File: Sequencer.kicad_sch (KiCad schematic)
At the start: 53 parts, among them J1 Screw_Terminal_01x12, J2 Serial_Mode, J3 USB_C_Receptacle_USB2.0_16P, J4 Extra, U1 ATtiny1616-S, U2 TLP3123, U3 TLP3123, U4 TLP3123, U5 TLP3123, U6 MC78L05_SOT89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

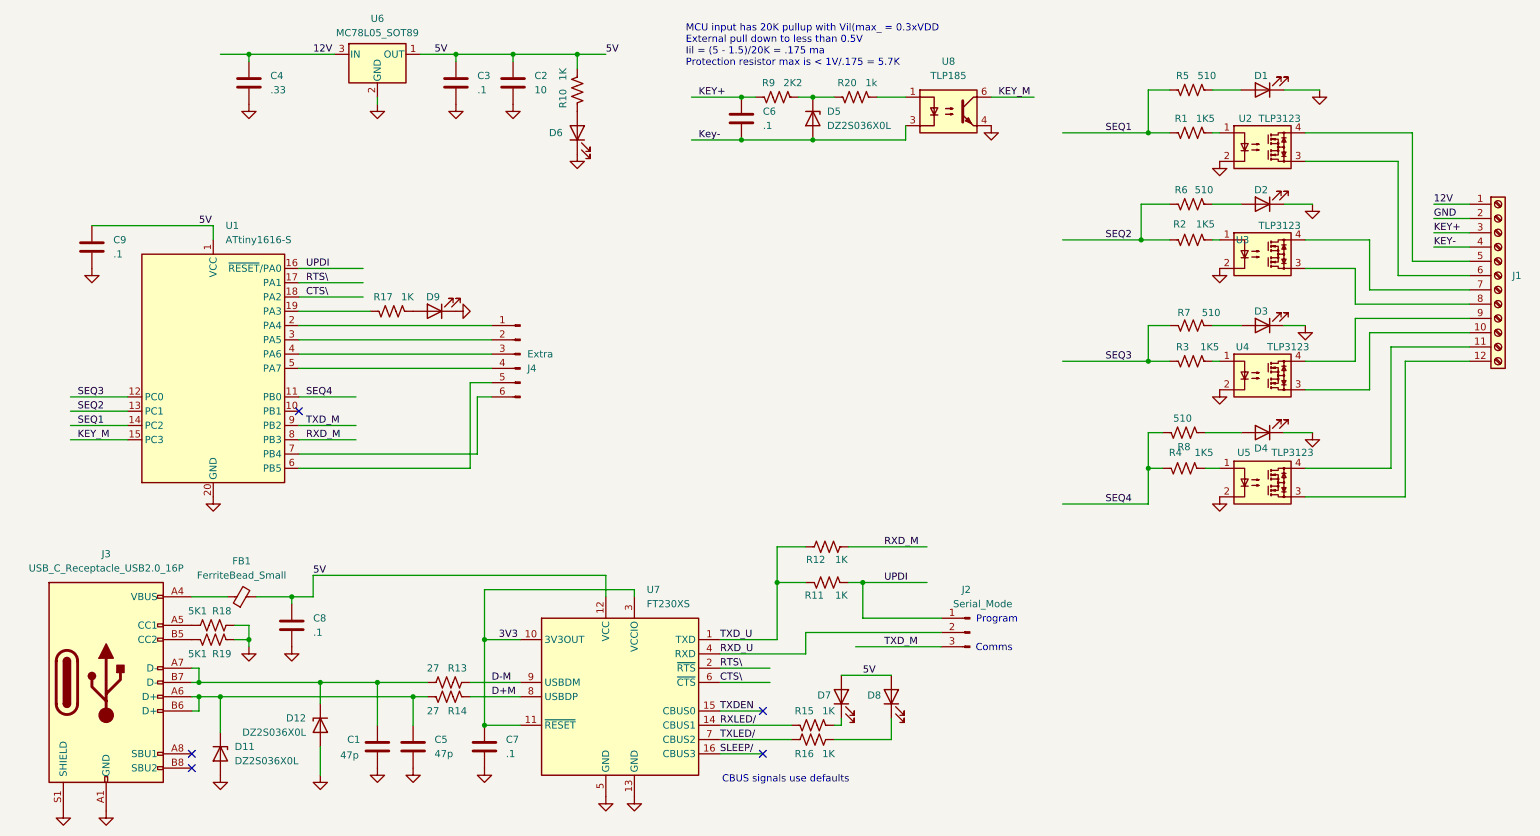
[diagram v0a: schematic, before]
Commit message: Finalized design for release to JCLPCB Add terminal block library Added some data sheets for terminal block, USB-C connector, etc
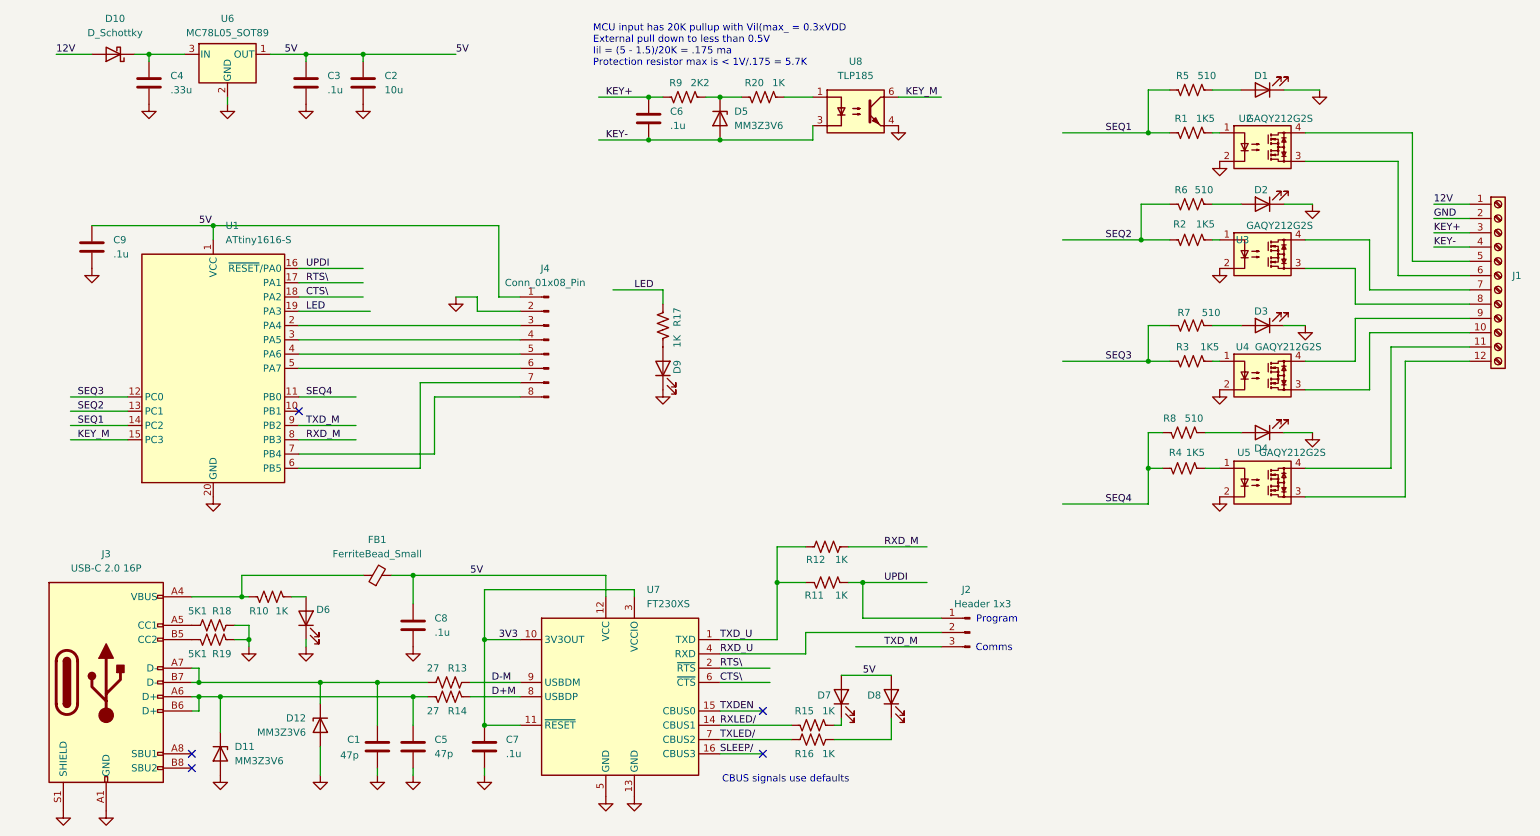
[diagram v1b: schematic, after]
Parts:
- removed J4: Extra, Connector_PinHeader_2.54mm:PinHeader_1x06_P2.54mm_Vertical, symbol Connector:Conn_01x06_Pin
- added D10: D_Schottky, Diode_SMD:D_0603_1608Metric, symbol Device:D_Schottky
- added J4: Conn_01x08_Pin, Connector_PinHeader_2.54mm:PinHeader_1x08_P2.54mm_Vertical, symbol Connector:Conn_01x08_Pin
- C1, C5: LCSC PN (none) -> C1671
- C2: value 10 -> 10u; LCSC PN (none) -> C19702
- C3, C6, C7, C8, C9: value .1 -> .1u; LCSC PN (none) -> C15849
- C4: value .33 -> .33u; LCSC PN (none) -> C2918485
- D1, D2, D3, D4: LCSC PN (none) -> C2286
- D11, D12, D5: value DZ2S036X0L -> MM3Z3V6; footprint Diode_SMD:D_SOD-523 -> Diode_SMD:D_SOD-323; LCSC PN (none) -> C19077454
- D6, D9: LCSC PN (none) -> C22371299
- D7, D8: LCSC PN (none) -> C72038
- FB1: LCSC PN (none) -> C1017
- J1: LCSC PN (none) -> C474929
- J2: value Serial_Mode -> Header 1x3; LCSC PN (none) -> C6332196
- J3: value USB_C_Receptacle_USB2.0_16P -> USB-C 2.0 16P; LCSC PN (none) -> C2835315
- R1, R2, R3, R4: LCSC PN (none) -> C22843
- R10, R11, R12, R15, R16, R17: LCSC PN (none) -> C21190
- R13, R14: LCSC PN (none) -> C25190
- R18, R19: LCSC PN (none) -> C23186
- R20: value 1k -> 1K; LCSC PN (none) -> C21190
- R5, R6, R7, R8: LCSC PN (none) -> C23193
- R9: LCSC PN (none) -> C4190
- U1: LCSC PN (none) -> C614136
- U2, U3, U4, U5: value TLP3123 -> GAQY212G2S; LCSC PN (none) -> C7435109
- U6: LCSC PN (none) -> C5346137
- U7: LCSC PN (none) -> C69082
- U8: LCSC PN (none) -> C17695768
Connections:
- net Key- is gone; now on net KEY-: C6.2, D5.2 (A), U8.3
- net 12V: now also D10.2 (A); no longer C4.1, U6.3 (IN)
- net 5V: now also J4.1 (Pin_1); no longer R10.2
- net GND: now also J4.2 (Pin_2)
- net LED: now reaches R17.1, U1.19 (PA3)
- net at U1.2 (PA4): now also J4.3 (Pin_3)
- net at U1.3 (PA5): now also J4.4 (Pin_4)
- net at U1.4 (PA6): now also J4.5 (Pin_5)
- net at U1.5 (PA7): now also J4.6 (Pin_6)
- net at U1.6 (PB5): now also J4.7 (Pin_7)
- net at U1.7 (PB4): now also J4.8 (Pin_8)
- net at FB1.1, J3.A4 (VBUS), J3.A9 (VBUS)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: now also R10.2
- new net: C4.1, D10.1 (K), U6.3 (IN)
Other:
- moved on the sheet: C2, C3, C4, C6, C8, D5, D6, FB1, R10, R20, R9, U6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

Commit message: Added USB-C connector footprints Changed ATTiny from SOIC-20 to 3x3 mm QFP
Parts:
- removed U1: ATtiny1616-S, Package_SO:SOIC-20W_7.5x12.8mm_P1.27mm, symbol MCU_Microchip_ATtiny:ATtiny1616-S
- added U9: ATtiny1616-M, Package_DFN_QFN:VQFN-20-1EP_3x3mm_P0.4mm_EP1.7x1.7mm, symbol MCU_Microchip_ATtiny:ATtiny1616-M
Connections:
- net 5V: now also U9.4 (VCC)
- net CTS\: now also U9.1 (PA2)
- net GND: now also R17.2, U9.21 (GND), U9.3 (GND); no longer D9.1 (K)
- net KEY_M: now also U9.18 (PC3)
- net LED: now also D9.2 (A), U9.2 (PA3); no longer R17.1
- net RTS\: now also U9.20 (PA1)
- net RXD_M: now also U9.11 (PB3)
- net SEQ1: now also U9.17 (PC2)
- net SEQ2: now also U9.16 (PC1)
- net SEQ3: now also U9.15 (PC0)
- net SEQ4: now also U9.14 (PB0)
- net TXD_M: now also U9.12 (PB2)
- net UPDI: now also U9.19 (~{RESET}/PA0)
- net X1: now reaches J4.3 (Pin_3)
- net X1: now also U9.5 (PA4)
- net X2: now reaches J4.4 (Pin_4)
- net X2: now also U9.6 (PA5)
- net X3: now reaches J4.5 (Pin_5)
- net X3: now also U9.7 (PA6)
- net X4: now reaches J4.6 (Pin_6)
- net X4: now also U9.8 (PA7)
- net X5: now reaches J4.7 (Pin_7)
- net X5: now also U9.9 (PB5)
- net X6: now reaches J4.8 (Pin_8)
- net X6: now also U9.10 (PB4)
- new net: D9.1 (K), R17.1
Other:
- moved on the sheet: D9, R17
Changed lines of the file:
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@@
 	(wire
 		(pts
-			(xy 129.54 66.04) (xy 129.54 68.58)
-		)
-		(stroke
-			(width 0)
-			(type default)
-		)
-	)
-	(wire
-		(pts
 			(xy 64.77 92.71) (xy 74.93 92.71)
 		)
@@
 	(wire
 		(pts
-			(xy 49.53 54.61) (xy 100.33 54.61)
+			(xy 49.53 54.61) (xy 99.06 54.61)
 		)
 		(stroke
@@
 	(wire
 		(pts
+			(xy 129.54 73.66) (xy 129.54 76.2)
+		)
+		(stroke
+			(width 0)
+			(type default)
+		)
+	)
+	(wire
+		(pts
 			(xy 151.13 31.75) (xy 156.21 31.75)
 		)
@@
 	(wire
 		(pts
-			(xy 100.33 67.31) (xy 104.14 67.31)
+			(xy 99.06 67.31) (xy 104.14 67.31)
 		)
 		(stroke
@@
 	(wire
 		(pts
-			(xy 100.33 54.61) (xy 100.33 67.31)
+			(xy 99.06 54.61) (xy 99.06 67.31)
 		)
 		(stroke
@@
 		)
 	)
+	(label "X5"
+		(at 100.33 82.55 0)
+		(fields_autoplaced yes)
+		(effects
+			(font
+				(size 1.27 1.27)
+			)
+			(justify left bottom)
+		)
+	)
 	(label "3V3"
 		(at 100.33 128.27 0)
@@
 		)
 	)
+	(label "X1"
+		(at 100.33 72.39 0)
+		(fields_autoplaced yes)
+		(effects
+			(font
+				(size 1.27 1.27)
+			)
+			(justify left bottom)
+		)
+	)
 	(label "KEY-"
 		(at 266.7 58.42 0)
@@
 		)
 	)
+	(label "X2"
+		(at 100.33 74.93 0)
+		(fields_autoplaced yes)
+		(effects
+			(font
+				(size 1.27 1.27)
+			)
+			(justify left bottom)
+		)
+	)
 	(label "KEY_M"
 		(at 172.72 31.75 0)
@@
 		)
 	)
+	(label "X3"
+		(at 100.33 77.47 0)
+		(fields_autoplaced yes)
+		(effects
+			(font
+				(size 1.27 1.27)
+			)
+			(justify left bottom)
+		)
+	)
+	(label "X4"
+		(at 100.33 80.01 0)
+		(fields_autoplaced yes)
+		(effects
+			(font
+				(size 1.27 1.27)
+			)
+			(justify left bottom)
+		)
+	)
 	(label "RXD_M"
 		(at 66.04 92.71 0)
@@
 		)
 	)
-	(symbol
-		(lib_id "MCU_Microchip_ATtiny:ATtiny1616-S")
-		(at 49.53 80.01 0)
-		(unit 1)
-		(exclude_from_sim no)
-		(in_bom yes)
-		(on_board yes)
-		(dnp no)
+	(label "X6"
+		(at 100.33 85.09 0)
 		(fields_autoplaced yes)
-		(property "Reference" "U1"
-			(at 51.7241 54.61 0)
-			(effects
-				(font
-					(size 1.27 1.27)
-				)
-				(justify left)
-			)
-		)
-		(property "Value" "ATtiny1616-S"
-			(at 51.7241 57.15 0)
-			(effects
-				(font
-					(size 1.27 1.27)
-				)
-				(justify left)
-			)
-		)
-		(property "Footprint" "Package_SO:SOIC-20W_7.5x12.8mm_P1.27mm"
-			(at 49.53 80.01 0)
-			(effects
-				(font
-					(size 1.27 1.27)
-					(italic yes)
-				)
-				(hide yes)
-			)
-		)
-		(property "Datasheet" "http://ww1.microchip.com/downloads/en/DeviceDoc/ATtiny3216_ATtiny1616-data-sheet-40001997B.pdf"
-			(at 49.53 80.01 0)
-			(effects
-				(font
-					(size 1.27 1.27)
-				)
-				(hide yes)
-			)
-		)
-		(property "Description" "20MHz, 16kB Flash, 2kB SRAM, 256B EEPROM, SOIC-20"
-			(at 49.53 80.01 0)
-			(effects
-				(font
-					(size 1.27 1.27)
-				)
-				(hide yes)
-			)
-		)
-		(property "LCSC PN" " C614136"
-			(at 49.53 80.01 0)
-			(effects
-				(font
-					(size 1.27 1.27)
-				)
-				(hide yes)
-			)
-		)
-		(pin "16"
-		)
-		(pin "14"
-		)
-		(pin "18"
-		)
-		(pin "20"
-		)
-		(pin "12"
-		)
-		(pin "15"
-		)
-		(pin "4"
-		)
-		(pin "19"
-		)
-		(pin "13"
-		)
-		(pin "11"
-		)
-		(pin "7"
-		)
-		(pin "8"
-		)
-		(pin "9"
-		)
-		(pin "1"
-		)
-		(pin "3"
-		)
-		(pin "17"
-		)
-		(pin "2"
-		)
-		(pin "10"
-		)
-		(pin "5"
-		)
-		(pin "6"
-		)
-		(instances
-			(project ""
-				(path "/3f7e4896-a5a1-43ac-9348-16f0feb459b4"
-					(reference "U1")
-					(unit 1)
-				)
+		(effects
+			(font
+				(size 1.27 1.27)
 			)
+			(justify left bottom)
 		)
 	)
@@
 	(symbol
 		(lib_id "Device:R_US")
-		(at 129.54 72.39 0)
+		(at 129.54 80.01 0)
 		(mirror y)
 		(unit 1)
@@
 		(dnp no)
 		(property "Reference" "R17"
-			(at 132.08 70.866 90)
+			(at 132.588 79.248 0)
 			(effects
 				(font
@@
 		)
 		(property "Value" "1K"
-			(at 132.08 75.184 90)
+			(at 132.08 81.28 0)
 			(effects
 				(font
@@
 		)
 		(property "Footprint" "Resistor_SMD:R_0603_1608Metric"
-			(at 128.524 72.644 90)
+			(at 128.524 80.264 90)
 			(effects
 				(font
@@
 		)
 		(property "Datasheet" "~"
-			(at 129.54 72.39 0)
+			(at 129.54 80.01 0)
 			(effects
 				(font
@@
 		)
 		(property "Description" "Resistor, US symbol"
-			(at 129.54 72.39 0)
+			(at 129.54 80.01 0)
 			(effects
 				(font
@@
 		)
 		(property "LCSC PN" "C21190"
-			(at 129.54 72.39 0)
+			(at 129.54 80.01 0)
 			(effects
 				(font
@@
 	(symbol
 		(lib_id "Device:LED")
-		(at 129.54 80.01 90)
+		(at 129.54 69.85 90)
 		(unit 1)
 		(exclude_from_sim no)
@@
 		(dnp no)
 		(property "Reference" "D9"
-			(at 132.08 79.756 0)
+			(at 132.08 69.596 90)
 			(effects
 				(font
@@
 		)
 		(property "Value" "Green"
-			(at 133.858 80.01 90)
+			(at 133.858 69.85 90)
 			(effects
 				(font
@@
 		)
 		(property "Footprint" "LED_SMD:LED_0603_1608Metric"
-			(at 129.54 80.01 0)
+			(at 129.54 69.85 0)
 			(effects
 				(font
@@
 		)
 		(property "Datasheet" "~"
-			(at 129.54 80.01 0)
+			(at 129.54 69.85 0)
 			(effects
 				(font
@@
 		)
 		(property "Description" "Light emitting diode"
-			(at 129.54 80.01 0)
+			(at 129.54 69.85 0)
 			(effects
 				(font
@@
 		)
 		(property "LCSC PN" " C22371299"
-			(at 129.54 80.01 0)
+			(at 129.54 69.85 0)
 			(effects
 				(font
@@
 					(unit 1)
 				)
+			)
+		)
+	)
+	(symbol
+		(lib_id "MCU_Microchip_ATtiny:ATtiny1616-M")
+		(at 49.53 80.01 0)
+		(unit 1)
+		(exclude_from_sim no)
+		(in_bom yes)
+		(on_board yes)
+		(dnp no)
+		(fields_autoplaced yes)
+		(property "Reference" "U9"
+			(at 51.7241 54.61 0)
+			(effects
+				(font
+					(size 1.27 1.27)
+				)
+				(justify left)
+			)
+		)
+		(property "Value" "ATtiny1616-M"
+			(at 51.7241 57.15 0)
+			(effects
+				(font
+					(size 1.27 1.27)
+				)
+				(justify left)
+			)
+		)
+		(property "Footprint" "Package_DFN_QFN:VQFN-20-1EP_3x3mm_P0.4mm_EP1.7x1.7mm"
+			(at 49.53 80.01 0)
+			(effects
+				(font
+					(size 1.27 1.27)
+					(italic yes)
+				)
+				(hide yes)
+			)
+		)
+		(property "Datasheet" "http://ww1.microchip.com/downloads/en/DeviceDoc/ATtiny3216_ATtiny1616-data-sheet-40001997B.pdf"
+			(at 49.53 80.01 0)
+			(effects
+				(font
+					(size 1.27 1.27)
+				)
+				(hide yes)
+			)
+		)
+		(property "Description" "20MHz, 16kB Flash, 2kB SRAM, 256B EEPROM, VQFN-20"
+			(at 49.53 80.01 0)
+			(effects
+				(font
+					(size 1.27 1.27)
+				)
+				(hide yes)
+			)
+		)
+		(pin "5"
+		)
+		(pin "7"
+		)
+		(pin "9"
+		)
+		(pin "1"
+		)
+		(pin "14"
+		)
+		(pin "18"
+		)
+		(pin "4"
+		)
+		(pin "3"
+		)
+		(pin "6"
+		)
+		(pin "8"
+		)
+		(pin "15"
+		)
+		(pin "17"
+		)
+		(pin "19"
+		)
+		(pin "21"
+		)
+		(pin "2"
+		)
+		(pin "10"
+		)
+		(pin "20"
+		)
+		(pin "11"
+		)
+		(pin "13"
+		)
+		(pin "12"
+		)
+		(pin "16"
+		)
+		(instances
+			(project ""
+				(path "/3f7e4896-a5a1-43ac-9348-16f0feb459b4"
+					(reference "U9")
+					(unit 1)
+				)
